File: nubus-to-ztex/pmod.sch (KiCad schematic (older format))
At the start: 2 parts, among them J9 Conn_02x06_Odd_Even

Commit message: cut down brightness of LEDs, more 2x32 pin headers reference
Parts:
- added C13: 100nF, Capacitor_SMD:C_0603_1608Metric, symbol Device:C
- added J10: Conn_01x06, For_SeeedStudio:PinSocket_1x06_P2.54mm_Vertical_For_SeeedStudio, symbol Connector_Generic:Conn_01x06
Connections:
- net labels added: LED0, LED1, LED2, LED3
- wire segments 7 -> 12
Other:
- note added: "Dual-row Pmod\nInternal, in line w/ the carrier"
- note added: "Single-row Pmod\nSharing the user LED signals, mostly for debugging\nInternal, perpendicular to carrier"
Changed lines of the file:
@@
 $Descr A4 11693 8268
 encoding utf-8
-Sheet 9 9
+Sheet 9 10
 Title "sbus-to-ztex blinkey stuff"
 Date ""
@@
 	6350 3000 6450 3000
 Connection ~ 6250 3200
+Wire Wire Line
+	5600 4400 5900 4400
+Wire Wire Line
+	5600 4500 6100 4500
+$Comp
+L power:GND #PWR0149
+U 1 1 63373073
+P 6100 4500
+F 0 "#PWR0149" H 6100 4250 50  0001 C CNN
+F 1 "GND" H 6105 4327 50  0000 C CNN
+F 2 "" H 6100 4500 50  0001 C CNN
+F 3 "" H 6100 4500 50  0001 C CNN
+	1    6100 4500
+	1    0    0    -1
+$EndComp
+$Comp
+L power:+3V3 #PWR0150
+U 1 1 63373079
+P 5900 4400
+F 0 "#PWR0150" H 5900 4250 50  0001 C CNN
+F 1 "+3V3" H 5915 4573 50  0000 C CNN
+F 2 "" H 5900 4400 50  0001 C CNN
+F 3 "" H 5900 4400 50  0001 C CNN
+	1    5900 4400
+	1    0    0    -1
+$EndComp
+$Comp
+L Device:C C?
+U 1 1 6337308E
+P 6100 4350
+AR Path="/5F679B53/6337308E" Ref="C?"  Part="1"
+AR Path="/5F6B165A/6337308E" Ref="C?"  Part="1"
+AR Path="/61631F14/6337308E" Ref="C?"  Part="1"
+AR Path="/62CC4C0A/6337308E" Ref="C13"  Part="1"
+F 0 "C13" H 6125 4450 50  0000 L CNN
+F 1 "100nF" H 6125 4250 50  0000 L CNN
+F 2 "Capacitor_SMD:C_0603_1608Metric" H 6138 4200 50  0001 C CNN
+F 3 "" H 6100 4350 50  0000 C CNN
+F 4 "www.yageo.com" H 6100 4350 50  0001 C CNN "MNF1_URL"
+F 5 "CC0603KRX7R8BB104" H 6100 4350 50  0001 C CNN "MPN"
+F 6 "603-CC603KRX7R8BB104" H 6100 4350 50  0001 C CNN "Mouser"
+F 7 "?" H 6100 4350 50  0001 C CNN "Digikey"
+F 8 "?" H 6100 4350 50  0001 C CNN "LCSC"
+F 9 "?" H 6100 4350 50  0001 C CNN "Koncar"
+F 10 "TB" H 6100 4350 50  0001 C CNN "Side"
+	1    6100 4350
+	1    0    0    -1
+$EndComp
+Connection ~ 6100 4500
+Wire Wire Line
+	5900 4400 6000 4400
+Wire Wire Line
+	6000 4400 6000 4200
+Wire Wire Line
+	6000 4200 6100 4200
+Connection ~ 5900 4400
+$Comp
+L Connector_Generic:Conn_01x06 J10
+U 1 1 63373341
+P 5400 4700
+F 0 "J10" H 5320 4175 50  0000 C CNN
+F 1 "Conn_01x06" H 5320 4266 50  0000 C CNN
+F 2 "For_SeeedStudio:PinSocket_1x06_P2.54mm_Vertical_For_SeeedStudio" H 5400 4700 50  0001 C CNN
+F 3 "~" H 5400 4700 50  0001 C CNN
+F 4 "A2541HWV-6P" H 5400 4700 50  0001 C CNN "MPN"
+F 5 "https://www.lcsc.com/product-detail/Female-Headers_CJT-Changjiang-Connectors-A2541HWV-6P_C2897443.html" H 5400 4700 50  0001 C CNN "URL"
+	1    5400 4700
+	-1   0    0    1
+$EndComp
+Text GLabel 5600 4600 2    60   Input ~ 12
+LED0
+Text GLabel 5600 4700 2    60   Input ~ 12
+LED1
+Text GLabel 5600 4800 2    60   Input ~ 12
+LED2
+Text GLabel 5600 4900 2    60   Input ~ 12
+LED3
+Text Notes 5400 2900 0    50   ~ 0
+Dual-row Pmod\nInternal, in line w/ the carrier
+Text Notes 4850 4150 0    50   ~ 0
+Single-row Pmod\nSharing the user LED signals, mostly for debugging\nInternal, perpendicular to carrier
 $EndSCHEMATC

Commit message: merge pmod & leds into an extended pmod on the outside. Also some BoM updates.
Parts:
- removed C13, C41: 100nF, Capacitor_SMD:C_0603_1608Metric, symbol Device:C
- removed J10: Conn_01x06, For_SeeedStudio:PinSocket_1x06_P2.54mm_Vertical_For_SeeedStudio, symbol Connector_Generic:Conn_01x06
- removed J9: Conn_02x06_Odd_Even, For_SeeedStudio:PinSocket_2x06_P2.54mm_Horizontal_For_SeeedStudio, symbol Connector_Generic:Conn_02x06_Odd_Even
- added C15: 100nF, Capacitor_SMD:C_0603_1608Metric, symbol Device:C
- added J8: Conn_02x08_Odd_Even, For_SeeedStudio:PinSocket_2x08_P2.54mm_Horizontal_ForSeeedStudio, symbol Connector_Generic:Conn_02x08_Odd_Even
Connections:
- net labels added: PMOD-13, PMOD-14, PMOD-15, PMOD-16
- net labels removed: LED0, LED1, LED2, LED3
- wire segments 12 -> 7
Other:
- note added: "Dual-row "extended" Pmod\nExternal, in line w/ the carrier"
- note added: "Extra Pins"
- note removed: "Dual-row Pmod\nInternal, in line w/ the carrier"
- note removed: "Single-row Pmod\nSharing the user LED signals, mostly for debugging\nInternal, perpendicular to carrier"
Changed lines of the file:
@@
 $Descr A4 11693 8268
 encoding utf-8
-Sheet 9 10
+Sheet 9 9
 Title "sbus-to-ztex blinkey stuff"
 Date ""
@@
 Comment4 ""
 $EndDescr
+Text Notes 7300 2850 0    50   ~ 0
+Dual-row "extended" Pmod\nExternal, in line w/ the carrier
 $Comp
-L Connector_Generic:Conn_02x06_Odd_Even J9
-U 1 1 618B4A38
-P 5650 3400
-F 0 "J9" H 5700 3817 50  0000 C CNN
-F 1 "Conn_02x06_Odd_Even" H 5700 3726 50  0000 C CNN
-F 2 "For_SeeedStudio:PinSocket_2x06_P2.54mm_Horizontal_For_SeeedStudio" H 5650 3400 50  0001 C CNN
-F 3 "~" H 5650 3400 50  0001 C CNN
-F 4 "A2541HWR-2x6P" H 5650 3400 50  0001 C CNN "MPN"
-F 5 "https://lcsc.com/product-detail/Pin-Header-Female-Header_Changjiang-Connectors-A2541HWR-2x6P_C239357.html" H 5650 3400 50  0001 C CNN "URL"
-	1    5650 3400
+L Connector_Generic:Conn_02x08_Odd_Even J8
+U 1 1 63467144
+P 7350 3600
+F 0 "J8" H 7400 4117 50  0000 C CNN
+F 1 "Conn_02x08_Odd_Even" H 7400 4026 50  0000 C CNN
+F 2 "For_SeeedStudio:PinSocket_2x08_P2.54mm_Horizontal_ForSeeedStudio" H 7350 3600 50  0001 C CNN
+F 3 "~" H 7350 3600 50  0001 C CNN
+F 4 "A2541HWR-2x8P" H 7350 3600 50  0001 C CNN "MPN"
+F 5 "https://www.lcsc.com/product-detail/Female-Headers_CJT-Changjiang-Connectors-A2541HWR-2x8P_C239359.html" H 7350 3600 50  0001 C CNN "URL"
+F 6 "PPPC082LJBN-RC" H 7350 3600 50  0001 C CNN "MPN-ALT"
+	1    7350 3600
 	1    0    0    -1
 $EndComp
+Text GLabel 7150 3500 0    50   Input ~ 0
+PMOD-5
+Text GLabel 7150 3600 0    50   Input ~ 0
+PMOD-7
+Text GLabel 7150 3700 0    50   Input ~ 0
+PMOD-9
+Text GLabel 7150 3800 0    50   Input ~ 0
+PMOD-11
+Text GLabel 7650 3800 2    50   Input ~ 0
+PMOD-12
+Text GLabel 7650 3500 2    50   Input ~ 0
+PMOD-6
+Text GLabel 7650 3600 2    50   Input ~ 0
+PMOD-8
+Text GLabel 7650 3700 2    50   Input ~ 0
+PMOD-10
 Wire Wire Line
-	5450 3200 5950 3200
+	7650 3300 7950 3300
 Wire Wire Line
-	5950 3200 6250 3200
-Connection ~ 5950 3200
-Wire Wire Line
-	5450 3300 5950 3300
-Wire Wire Line
-	5950 3300 6450 3300
-Connection ~ 5950 3300
+	7650 3400 8150 3400
 $Comp
-L power:GND #PWR0129
-U 1 1 618B4A45
-P 6450 3300
-F 0 "#PWR0129" H 6450 3050 50  0001 C CNN
-F 1 "GND" H 6455 3127 50  0000 C CNN
-F 2 "" H 6450 3300 50  0001 C CNN
-F 3 "" H 6450 3300 50  0001 C CNN
-	1    6450 3300
+L power:GND #PWR0151
+U 1 1 634673C0
+P 8150 3400
+F 0 "#PWR0151" H 8150 3150 50  0001 C CNN
+F 1 "GND" H 8155 3227 50  0000 C CNN
+F 2 "" H 8150 3400 50  0001 C CNN
+F 3 "" H 8150 3400 50  0001 C CNN
+	1    8150 3400
 	1    0    0    -1
 $EndComp
 $Comp
-L power:+3V3 #PWR0130
-U 1 1 618B4A4B
-P 6250 3200
-F 0 "#PWR0130" H 6250 3050 50  0001 C CNN
-F 1 "+3V3" H 6265 3373 50  0000 C CNN
-F 2 "" H 6250 3200 50  0001 C CNN
-F 3 "" H 6250 3200 50  0001 C CNN
-	1    6250 3200
-	1    0    0    -1
-$EndComp
-Text GLabel 5950 3700 2    50   Input ~ 0
-PMOD-12
-Text GLabel 5450 3400 0    50   Input ~ 0
-PMOD-5
-Text GLabel 5950 3400 2    50   Input ~ 0
-PMOD-6
-Text GLabel 5450 3500 0    50   Input ~ 0
-PMOD-7
-Text GLabel 5950 3500 2    50   Input ~ 0
-PMOD-8
-Text GLabel 5450 3600 0    50   Input ~ 0
-PMOD-9
-Text GLabel 5950 3600 2    50   Input ~ 0
-PMOD-10
-Text GLabel 5450 3700 0    50   Input ~ 0
-PMOD-11
-$Comp
-L Device:C C?
-U 1 1 618B4A60
-P 6450 3150
-AR Path="/5F679B53/618B4A60" Ref="C?"  Part="1"
-AR Path="/5F6B165A/618B4A60" Ref="C?"  Part="1"
-AR Path="/61631F14/618B4A60" Ref="C41"  Part="1"
-AR Path="/62CC4C0A/618B4A60" Ref="C12"  Part="1"
-F 0 "C12" H 6475 3250 50  0000 L CNN
-F 1 "100nF" H 6475 3050 50  0000 L CNN
-F 2 "Capacitor_SMD:C_0603_1608Metric" H 6488 3000 50  0001 C CNN
-F 3 "" H 6450 3150 50  0000 C CNN
-F 4 "www.yageo.com" H 6450 3150 50  0001 C CNN "MNF1_URL"
-F 5 "CC0603KRX7R8BB104" H 6450 3150 50  0001 C CNN "MPN"
-F 6 "603-CC603KRX7R8BB104" H 6450 3150 50  0001 C CNN "Mouser"
-F 7 "?" H 6450 3150 50  0001 C CNN "Digikey"
-F 8 "?" H 6450 3150 50  0001 C CNN "LCSC"
-F 9 "?" H 6450 3150 50  0001 C CNN "Koncar"
-F 10 "TB" H 6450 3150 50  0001 C CNN "Side"
-	1    6450 3150
-	1    0    0    -1
-$EndComp
-Connection ~ 6450 3300
-Wire Wire Line
-	6250 3200 6350 3200
-Wire Wire Line
-	6350 3200 6350 3000
-Wire Wire Line
-	6350 3000 6450 3000
-Connection ~ 6250 3200
-Wire Wire Line
-	5600 4400 5900 4400
-Wire Wire Line
-	5600 4500 6100 4500
-$Comp
-L power:GND #PWR0149
-U 1 1 63373073
-P 6100 4500
-F 0 "#PWR0149" H 6100 4250 50  0001 C CNN
-F 1 "GND" H 6105 4327 50  0000 C CNN
-F 2 "" H 6100 4500 50  0001 C CNN
-F 3 "" H 6100 4500 50  0001 C CNN
-	1    6100 4500
-	1    0    0    -1
-$EndComp
-$Comp
-L power:+3V3 #PWR0150
-U 1 1 63373079
-P 5900 4400
-F 0 "#PWR0150" H 5900 4250 50  0001 C CNN
-F 1 "+3V3" H 5915 4573 50  0000 C CNN
-F 2 "" H 5900 4400 50  0001 C CNN
-F 3 "" H 5900 4400 50  0001 C CNN
-	1    5900 4400
+L power:+3V3 #PWR0152
+U 1 1 634673C6
+P 7950 3300
+F 0 "#PWR0152" H 7950 3150 50  0001 C CNN
+F 1 "+3V3" H 7965 3473 50  0000 C CNN
+F 2 "" H 7950 3300 50  0001 C CNN
+F 3 "" H 7950 3300 50  0001 C CNN
+	1    7950 3300
 	1    0    0    -1
 $EndComp
 $Comp
 L Device:C C?
-U 1 1 6337308E
-P 6100 4350
-AR Path="/5F679B53/6337308E" Ref="C?"  Part="1"
-AR Path="/5F6B165A/6337308E" Ref="C?"  Part="1"
-AR Path="/61631F14/6337308E" Ref="C?"  Part="1"
-AR Path="/62CC4C0A/6337308E" Ref="C13"  Part="1"
-F 0 "C13" H 6125 4450 50  0000 L CNN
-F 1 "100nF" H 6125 4250 50  0000 L CNN
-F 2 "Capacitor_SMD:C_0603_1608Metric" H 6138 4200 50  0001 C CNN
-F 3 "" H 6100 4350 50  0000 C CNN
-F 4 "www.yageo.com" H 6100 4350 50  0001 C CNN "MNF1_URL"
-F 5 "CC0603KRX7R8BB104" H 6100 4350 50  0001 C CNN "MPN"
-F 6 "603-CC603KRX7R8BB104" H 6100 4350 50  0001 C CNN "Mouser"
-F 7 "?" H 6100 4350 50  0001 C CNN "Digikey"
-F 8 "?" H 6100 4350 50  0001 C CNN "LCSC"
-F 9 "?" H 6100 4350 50  0001 C CNN "Koncar"
-F 10 "TB" H 6100 4350 50  0001 C CNN "Side"
-	1    6100 4350
+U 1 1 634673D3
+P 8150 3250
+AR Path="/5F679B53/634673D3" Ref="C?"  Part="1"
+AR Path="/5F6B165A/634673D3" Ref="C?"  Part="1"
+AR Path="/61631F14/634673D3" Ref="C?"  Part="1"
+AR Path="/62CC4C0A/634673D3" Ref="C15"  Part="1"
+F 0 "C15" H 8175 3350 50  0000 L CNN
+F 1 "100nF" H 8175 3150 50  0000 L CNN
+F 2 "Capacitor_SMD:C_0603_1608Metric" H 8188 3100 50  0001 C CNN
+F 3 "" H 8150 3250 50  0000 C CNN
+F 4 "www.yageo.com" H 8150 3250 50  0001 C CNN "MNF1_URL"
+F 5 "CC0603KRX7R8BB104" H 8150 3250 50  0001 C CNN "MPN"
+F 6 "603-CC603KRX7R8BB104" H 8150 3250 50  0001 C CNN "Mouser"
+F 7 "?" H 8150 3250 50  0001 C CNN "Digikey"
+F 8 "?" H 8150 3250 50  0001 C CNN "LCSC"
+F 9 "?" H 8150 3250 50  0001 C CNN "Koncar"
+F 10 "TB" H 8150 3250 50  0001 C CNN "Side"
+F 11 "https://lcsc.com/product-detail/Multilayer-Ceramic-Capacitors-MLCC-SMD-SMT_YAGEO-CC0603KRX7R8BB104_C92490.html" H 3000 6050 50  0001 C CNN "URL"
+	1    8150 3250
 	1    0    0    -1
 $EndComp
-Connection ~ 6100 4500
+Connection ~ 8150 3400
 Wire Wire Line
-	5900 4400 6000 4400
+	7950 3300 8050 3300
 Wire Wire Line
-	6000 4400 6000 4200
+	8050 3300 8050 3100
 Wire Wire Line
-	6000 4200 6100 4200
-Connection ~ 5900 4400
-$Comp
-L Connector_Generic:Conn_01x06 J10
-U 1 1 63373341
-P 5400 4700
-F 0 "J10" H 5320 4175 50  0000 C CNN
-F 1 "Conn_01x06" H 5320 4266 50  0000 C CNN
-F 2 "For_SeeedStudio:PinSocket_1x06_P2.54mm_Vertical_For_SeeedStudio" H 5400 4700 50  0001 C CNN
-F 3 "~" H 5400 4700 50  0001 C CNN
-F 4 "A2541HWV-6P" H 5400 4700 50  0001 C CNN "MPN"
-F 5 "https://www.lcsc.com/product-detail/Female-Headers_CJT-Changjiang-Connectors-A2541HWV-6P_C2897443.html" H 5400 4700 50  0001 C CNN "URL"
-	1    5400 4700
-	-1   0    0    1
-$EndComp
-Text GLabel 5600 4600 2    60   Input ~ 12
-LED0
-Text GLabel 5600 4700 2    60   Input ~ 12
-LED1
-Text GLabel 5600 4800 2    60   Input ~ 12
-LED2
-Text GLabel 5600 4900 2    60   Input ~ 12
-LED3
-Text Notes 5400 2900 0    50   ~ 0
-Dual-row Pmod\nInternal, in line w/ the carrier
-Text Notes 4850 4150 0    50   ~ 0
-Single-row Pmod\nSharing the user LED signals, mostly for debugging\nInternal, perpendicular to carrier
+	8050 3100 8150 3100
+Connection ~ 7950 3300
+Wire Wire Line
+	7150 3300 7650 3300
+Connection ~ 7650 3300
+Wire Wire Line
+	7650 3400 7150 3400
+Connection ~ 7650 3400
+Text GLabel 7650 3900 2    50   Input ~ 0
+PMOD-14
+Text GLabel 7650 4000 2    50   Input ~ 0
+PMOD-16
+Text GLabel 7150 3900 0    50   Input ~ 0
+PMOD-13
+Text GLabel 7150 4000 0    50   Input ~ 0
+PMOD-15
+Wire Notes Line
+	6700 3850 8100 3850
+Wire Notes Line
+	8100 3850 8100 4050
+Wire Notes Line
+	8100 4050 6700 4050
+Wire Notes Line
+	6700 4050 6700 3850
+Text Notes 8100 4050 0    50   ~ 0
+Extra Pins
 $EndSCHEMATC

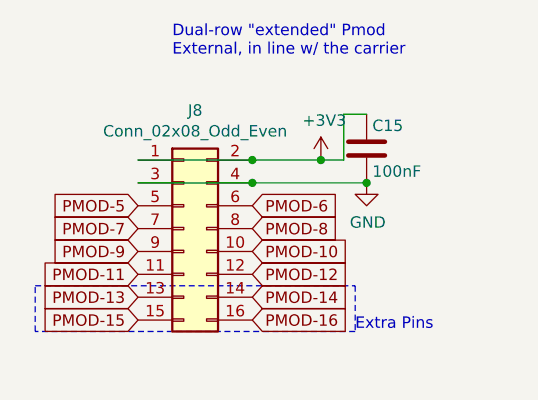
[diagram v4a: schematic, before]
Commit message: more update to V1.2 to try to limit cost
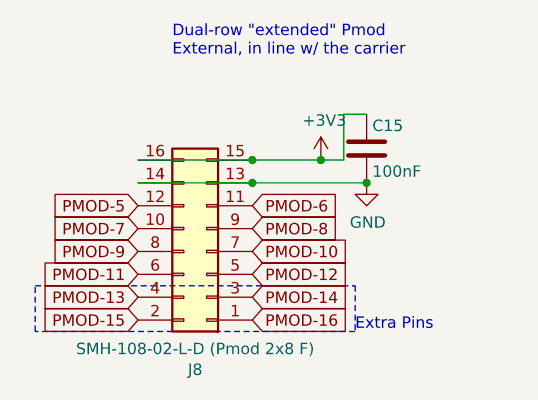
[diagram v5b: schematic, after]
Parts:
- J8: value Conn_02x08_Odd_Even -> SMH-108-02-L-D (Pmod 2x8 F); footprint For_SeeedStudio:PinSocket_2x08_P2.54mm_Horizontal_ForSeeedStudio -> For_SeeedStudio:SAMTEC-SMH-108-02-X-D; MPN A2541HWR-2x8P -> SMH-108-02-L-D; MPN-ALT PPPC082LJBN-RC -> (none); URL https://www.lcsc.com/product-detail/Female-Headers_CJT-Chan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 -> https://www.mouser.fr/ProductDetail/Samtec/SMH-108-02-L-D?q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
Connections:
- net +3V3: now also J8.15 (Pin_15), J8.16 (Pin_16); no longer J8.1 (Pin_1), J8.2 (Pin_2)
- net GND: now also J8.13 (Pin_13), J8.14 (Pin_14); no longer J8.3 (Pin_3), J8.4 (Pin_4)
- net PMOD-10: now also J8.7 (Pin_7); no longer J8.10 (Pin_10)
- net PMOD-11: now also J8.6 (Pin_6); no longer J8.11 (Pin_11)
- net PMOD-12: now also J8.5 (Pin_5); no longer J8.12 (Pin_12)
- net PMOD-13: now also J8.4 (Pin_4); no longer J8.13 (Pin_13)
- net PMOD-14: now also J8.3 (Pin_3); no longer J8.14 (Pin_14)
- net PMOD-15: now also J8.2 (Pin_2); no longer J8.15 (Pin_15)
- net PMOD-16: now also J8.1 (Pin_1); no longer J8.16 (Pin_16)
- net PMOD-5: now also J8.12 (Pin_12); no longer J8.5 (Pin_5)
- net PMOD-6: now also J8.11 (Pin_11); no longer J8.6 (Pin_6)
- net PMOD-7: now also J8.10 (Pin_10); no longer J8.7 (Pin_7)
- net PMOD-8: now also J8.9 (Pin_9); no longer J8.8 (Pin_8)
- net PMOD-9: now also J8.8 (Pin_8); no longer J8.9 (Pin_9)
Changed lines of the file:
@@
 $Descr A4 11693 8268
 encoding utf-8
-Sheet 9 8
+Sheet 8 8
 Title "sbus-to-ztex blinkey stuff"
 Date ""
@@
 L Connector_Generic:Conn_02x08_Odd_Even J8
 U 1 1 63467144
-P 7350 3600
-F 0 "J8" H 7400 4117 50  0000 C CNN
-F 1 "Conn_02x08_Odd_Even" H 7400 4026 50  0000 C CNN
-F 2 "For_SeeedStudio:PinSocket_2x08_P2.54mm_Horizontal_ForSeeedStudio" H 7350 3600 50  0001 C CNN
-F 3 "~" H 7350 3600 50  0001 C CNN
-F 4 "A2541HWR-2x8P" H 7350 3600 50  0001 C CNN "MPN"
-F 5 "https://www.lcsc.com/product-detail/Female-Headers_CJT-Changjiang-Connectors-A2541HWR-2x8P_C239359.html" H 7350 3600 50  0001 C CNN "URL"
-F 6 "PPPC082LJBN-RC" H 7350 3600 50  0001 C CNN "MPN-ALT"
-	1    7350 3600
-	1    0    0    -1
+P 7450 3700
+F 0 "J8" H 7500 4217 50  0000 C CNN
+F 1 "SMH-108-02-L-D (Pmod 2x8 F)" H 7500 4126 50  0000 C CNN
+F 2 "For_SeeedStudio:SAMTEC-SMH-108-02-X-D" H 7450 3700 50  0001 C CNN
+F 3 "~" H 7450 3700 50  0001 C CNN
+F 4 "SMH-108-02-L-D" H 7450 3700 50  0001 C CNN "MPN"
+F 5 "https://www.mouser.fr/ProductDetail/Samtec/SMH-108-02-L-D?qs=%252BZP6%2F%252BtExtAyrMiVCu9Apg%3D%3D" H 7450 3700 50  0001 C CNN "URL"
+	1    7450 3700
+	-1   0    0    1
 $EndComp
 Text GLabel 7150 3500 0    50   Input ~ 0
@@
 Text GLabel 7650 3700 2    50   Input ~ 0
 PMOD-10
-Wire Wire Line
-	7650 3300 7950 3300
-Wire Wire Line
-	7650 3400 8150 3400
 $Comp
 L power:GND #PWR0151
@@
 	1    0    0    -1
 $EndComp
-Connection ~ 8150 3400
 Wire Wire Line
 	7950 3300 8050 3300
@@
 Wire Wire Line
 	8050 3100 8150 3100
-Connection ~ 7950 3300
-Wire Wire Line
-	7150 3300 7650 3300
-Connection ~ 7650 3300
-Wire Wire Line
-	7650 3400 7150 3400
-Connection ~ 7650 3400
 Text GLabel 7650 3900 2    50   Input ~ 0
 PMOD-14
@@
 Text Notes 8100 4050 0    50   ~ 0
 Extra Pins
+Wire Wire Line
+	7150 3300 7650 3300
+Wire Wire Line
+	7650 3300 7950 3300
+Connection ~ 7650 3300
+Connection ~ 7950 3300
+Wire Wire Line
+	7150 3400 7650 3400
+Wire Wire Line
+	7650 3400 8150 3400
+Connection ~ 7650 3400
+Connection ~ 8150 3400
 $EndSCHEMATC

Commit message: minor cleanups
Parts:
- C15: LCSC ? -> (none)
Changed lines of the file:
@@
 F 6 "603-CC603KRX7R8BB104" H 8150 3250 50  0001 C CNN "Mouser"
 F 7 "?" H 8150 3250 50  0001 C CNN "Digikey"
-F 8 "?" H 8150 3250 50  0001 C CNN "LCSC"
+F 8 "" H 8150 3250 50  0001 C CNN "LCSC"
 F 9 "?" H 8150 3250 50  0001 C CNN "Koncar"
 F 10 "TB" H 8150 3250 50  0001 C CNN "Side"

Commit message: BoM, power plane, serial back to THT, ...
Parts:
- C15: URL https://lcsc.com/product-detail/Multilayer-Ceramic-Capacito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 -> https://www.lcsc.com/product-detail/Multilayer-Ceramic-Capa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
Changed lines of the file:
@@
 F 9 "?" H 8150 3250 50  0001 C CNN "Koncar"
 F 10 "TB" H 8150 3250 50  0001 C CNN "Side"
-F 11 "https://lcsc.com/product-detail/Multilayer-Ceramic-Capacitors-MLCC-SMD-SMT_YAGEO-CC0603KRX7R8BB104_C92490.html" H 3000 6050 50  0001 C CNN "URL"
+F 11 "https://www.lcsc.com/product-detail/Multilayer-Ceramic-Capacitors-MLCC-SMD-SMT_YAGEO-CC0603KRX7R8BB104_C92490.html" H 3000 6050 50  0001 C CNN "URL"
 	1    8150 3250
 	1    0    0    -1
